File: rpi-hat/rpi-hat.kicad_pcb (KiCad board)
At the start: 2 copper layers, 65 x 56.5 mm, 32 parts, among them J1 Raspberry_Pi_2_3, J2 UEXT_Slave, J3 RJ45_Shielded, J4 DB9 Male CAN, J5 Screw_Terminal_01x02, U1 CAT24C128, U2 MCP2517FD-xSL, U3 SN65HVD235, Y1 20MHz

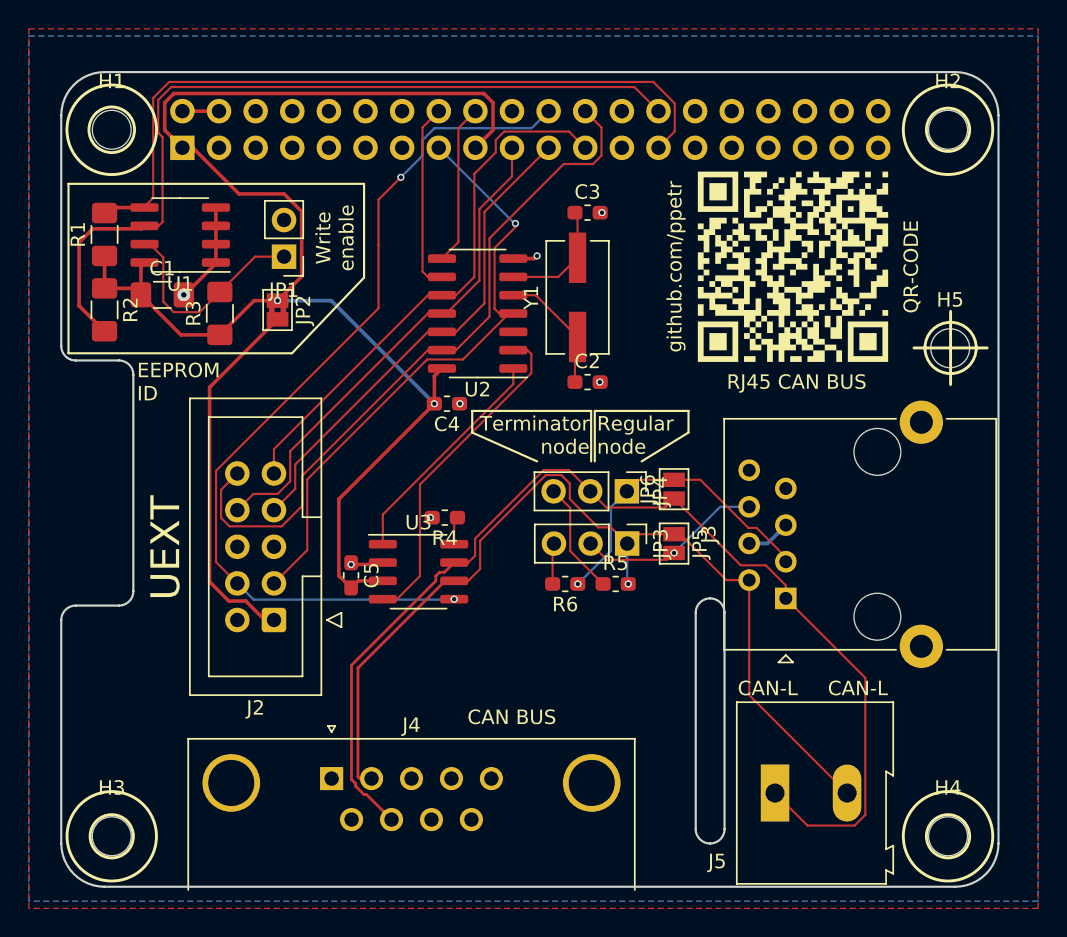
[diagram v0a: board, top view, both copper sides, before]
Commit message: Fix problems with project-specific library
Use 1206/3216Metric footprints for all capacitors and resistors.
Fix QR code to be negative and to point to the proper address.
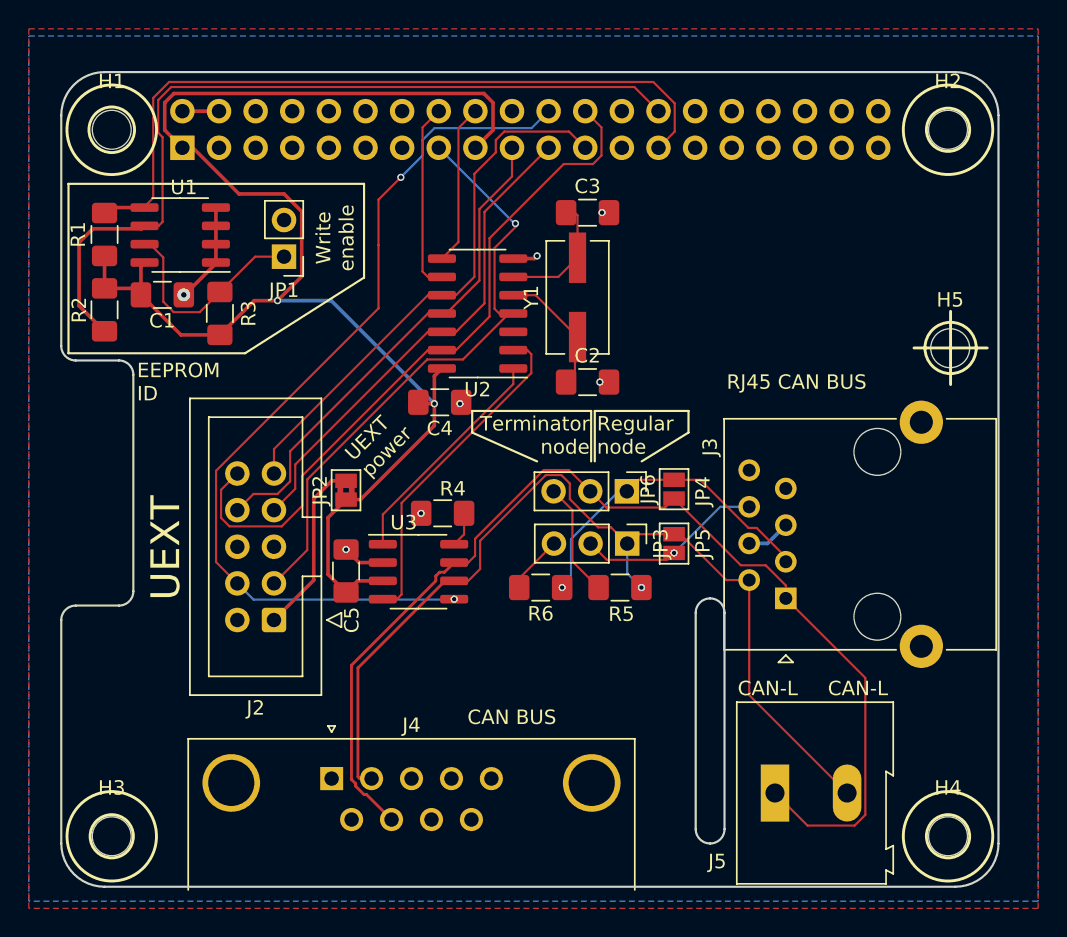
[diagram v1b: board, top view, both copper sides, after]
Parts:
- removed QR-CODE: github.com/ppetr, rpi-hat:github.com_ppetr
- C2, C3, C4, C5: footprint Capacitor_SMD:C_0603_1608Metric_Pad1.05x0.95mm_HandSolder -> Capacitor_SMD:C_1206_3216Metric_Pad1.42x1.75mm_HandSolder
- R4, R5, R6: footprint Resistor_SMD:R_0603_1608Metric_Pad1.05x0.95mm_HandSolder -> Resistor_SMD:R_1206_3216Metric_Pad1.42x1.75mm_HandSolder
- moved JP2 13.4 mm to (48.8, 50.0), turned to 90 degrees
- moved R6 1.72 mm to (62.2, 56.8)
- moved C4 0.51 mm to (55.2, 43.9)
- moved C5 0.46 mm to (48.8, 55.6)
- moved R5 0.39 mm to (67.8, 56.8)
- moved R4 0.34 mm to (55.5, 51.6)
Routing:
- net /UEXT_POWER: track 25.7 -> 12.3 mm
- net +3V3: track 101.5 -> 104.5 mm
- net Net-(JP3-Pad3): track 2.84 -> 4.05 mm
- net /CAN2+: track 21.7 -> 22.8 mm
- net CAN-: track 67.1 -> 67.6 mm
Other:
- board text added: "UEXT power"
